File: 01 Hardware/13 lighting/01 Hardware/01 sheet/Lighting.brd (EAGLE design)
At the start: 69 x 80 mm, 58 parts, among them IC1 AD822R, IC2 AD822R, J2 614105150721, J3 690367290476, J4 690367291276, U10 Grün, U11 Rot, U7 W1, U8 W2

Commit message: new Lighting PCB
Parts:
- removed J2: 614105150721, Eagle_WR-USB (rev24c):614105150721
- added J1: 614105150621, Eagle_WR-USB (rev25c):614105150621
- GRUEN: value (none) -> GRUEN
- ROT: value (none) -> ROT
- U$1: value RP2350_STAMPTHT -> RP2350_STAMPSMD; device rp2xxx_stamp:RP2XXX_STAMP_TH -> rp2xxx_stamp:RP2XXX_STAMP_SMD
- W11: value (none) -> W11
- W12: value (none) -> W12
- W13: value (none) -> W13
- W21: value (none) -> W21
- W22: value (none) -> W22
- W23: value (none) -> W23
- moved J3 30.5 mm to (34.0, 60.8), turned to 180 degrees
- moved J4 27.9 mm to (55.7, 39.3), turned to 90 degrees
- moved D3 21.9 mm to (35.0, 47.5), turned to 90 degrees
- moved C5 6.96 mm to (17.7, 59.3), turned to 270 degrees
- moved D2 6.84 mm to (20.4, 57.5)
- moved R8 6.84 mm to (23.9, 59.0)
- moved R7 4.23 mm to (15.2, 59.3), turned to 90 degrees
- moved C6 1.27 mm to (17.0, 53.2)
- moved C2 1.27 mm to (8.27, 34.5)
- moved D8 1.27 mm to (11.3, 35.5)
- moved R3 1.27 mm to (8.27, 37.0)
- moved U$1 0.71 mm to (34.8, 40.5), turned to 0 degrees
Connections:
- net +3V3: no longer U$1.TH34
- net +5V: now also D5.1; no longer D5.2, U$1.TH33
- net ADC0: no longer U$1.TH27
- net ADC1: no longer U$1.TH28
- net ADC2: no longer U$1.TH29
- net ADC3: no longer U$1.TH30
- net D+@1: now also J1.3; no longer J2.3
- net D-@1: now also J1.2; no longer J2.2
- net D_N: no longer U$1.TH35
- net D_P: no longer U$1.TH36
- net GND: now also GRUEN.5, J1.5, J1.S1, J1.S2, ROT.5, W11.5, W12.5, W13.5, W21.5, W22.5, W23.5; no longer J2.5, U$1.TH31
- net N$11: no longer U$1.TH8
- net N$12: no longer U$1.TH7
- net N$14: no longer U$1.TH6
- net N$21: no longer U$1.TH2
- net N$22: no longer U$1.TH1
- net N$4: no longer U$1.TH10
- net N$6: no longer U$1.TH9
- net PD_W1: no longer W12.4, W13.4
- net PD_W2: no longer W21.4, W22.4
- net PWM_G: no longer U$1.TH22
- net PWM_R: no longer U$1.TH25
- net PWM_W1: no longer U$1.TH23
- net PWM_W2: no longer U$1.TH24
- net VBAT: no longer U$1.TH32
- net VBUS: now also D5.2, J1.1; no longer D5.1, J2.1
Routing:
- net PD_W2: track 154.2 -> 25.7 mm, vias 5 -> 1
- net PD_W1: track 159.7 -> 32.2 mm, vias 2 -> 1
- net +5V: track 77.5 -> 129.3 mm, vias 2 -> 3
- net ADC3: track 63.6 -> 18.3 mm, vias 1 -> 2
- net N$21: track 67.3 -> 26.9 mm, vias 1 -> 2
- net VBUS: track 8.17 -> 34.7 mm, vias 1 -> 2
- net GND: track 417.9 -> 391.6 mm, vias 20 -> 9
- net PWM_W1: track 44.3 -> 20.0 mm, vias 3 -> 1
- net ADC2: track 37.4 -> 13.1 mm
- net LED-W1-: track 84.8 -> 60.6 mm
- net PWM_G: track 33.8 -> 53.0 mm, vias 1 -> 3
- net PWM_R: track 11.0 -> 27.2 mm, vias 0 -> 1
- net ADC1: track 39.6 -> 25.1 mm
- net W21_W22: track 74.3 -> 87.5 mm, vias 2 -> 0
- net +12V: track 213.2 -> 226.1 mm, vias 3 -> 6
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
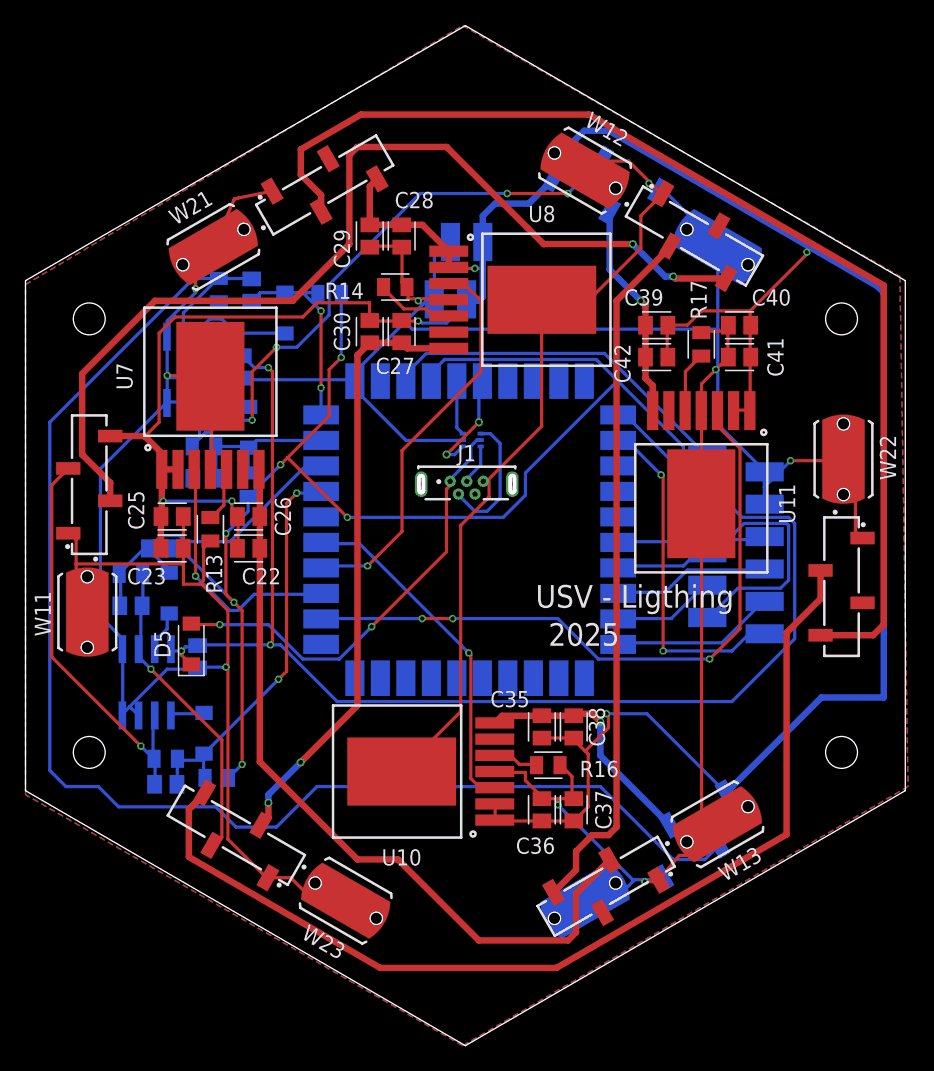
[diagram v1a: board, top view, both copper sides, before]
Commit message: new Pinlayout (LED-Board)
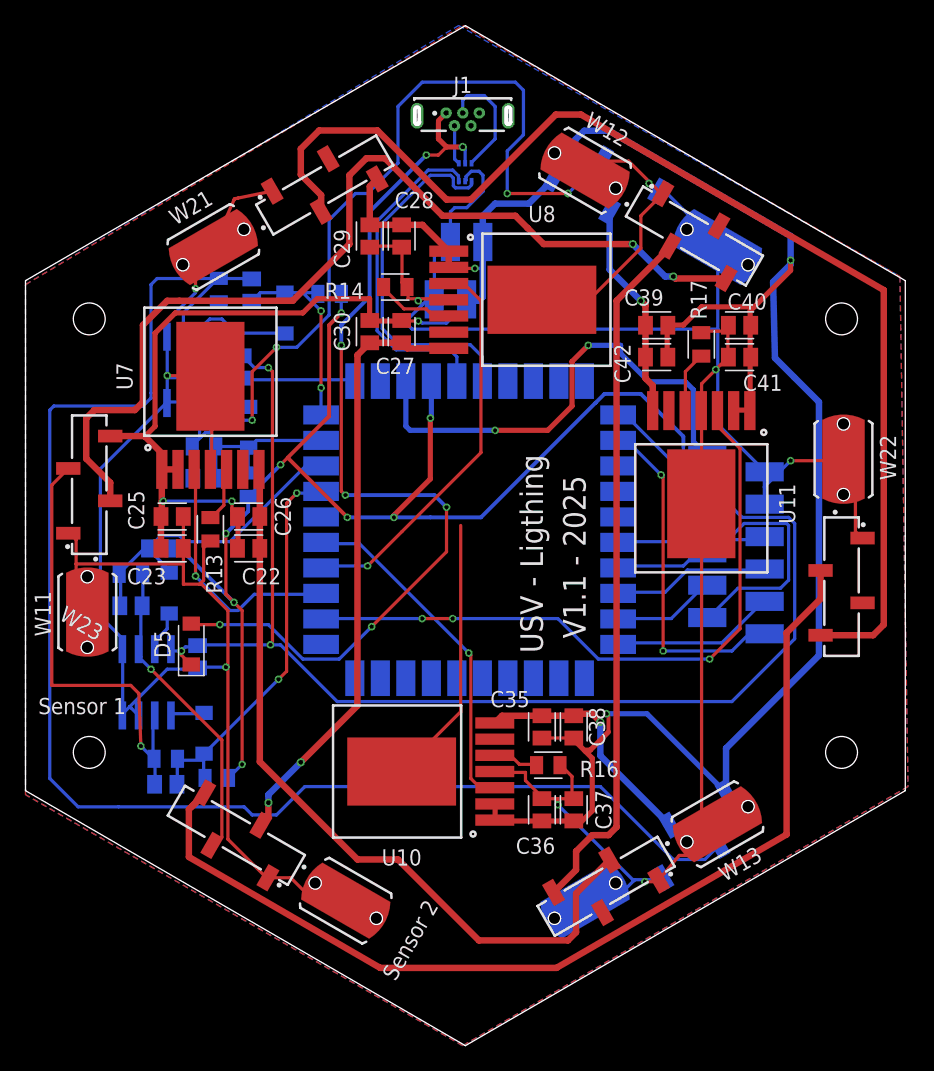
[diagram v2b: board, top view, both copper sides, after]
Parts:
- moved J1 28.9 mm to (34.3, 73.0)
- moved D3 21.0 mm to (34.5, 68.5), turned to 0 degrees
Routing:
- net VBUS: track 34.7 -> 73.7 mm, vias 2 -> 7
- net GND: track 391.6 -> 363.7 mm
- net D_N: track 4.31 -> 26.7 mm
- net D_P: track 8.48 -> 29.0 mm, vias 2 -> 0
- net PD_R: track 50.5 -> 69.9 mm
- net +5V: track 129.3 -> 140.3 mm, vias 3 -> 5
- net D-@1: track 10.5 -> 3.09 mm
- net +12V: track 226.1 -> 219.3 mm
- net D+@1: track 3.25 -> 9.27 mm
- net PD_G: track 112.2 -> 117.5 mm
- net +3V3: track 113.1 -> 108.0 mm, vias 6 -> 8
- net W21_W22: track 87.5 -> 92.1 mm
- net PD_W1: track 32.2 -> 35.8 mm
- net W11_W12: track 77.1 -> 76.5 mm
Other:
- board text added: "Sensor 1"
- board text added: "Sensor 2"
- board text added: "V1.1 - 2025"
- board text removed: "2025"
